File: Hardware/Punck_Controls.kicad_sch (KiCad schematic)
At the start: 38 parts, among them J1 Conn_01x12_Female, J10 Conn_01x12_Female, J11 Tempo_Out, J12 USB_B_Micro, J13 Midi_In_L, J14 Audio_Out_L, J15 Audio_Out_R, J2 Conn_01x12_Female, J3 Conn_01x12_Female, J4 Kick_In, J5 Snare_In, J6 CH_In, J7 OH_In, J8 SamplerA_In, J9 SamplerB_In

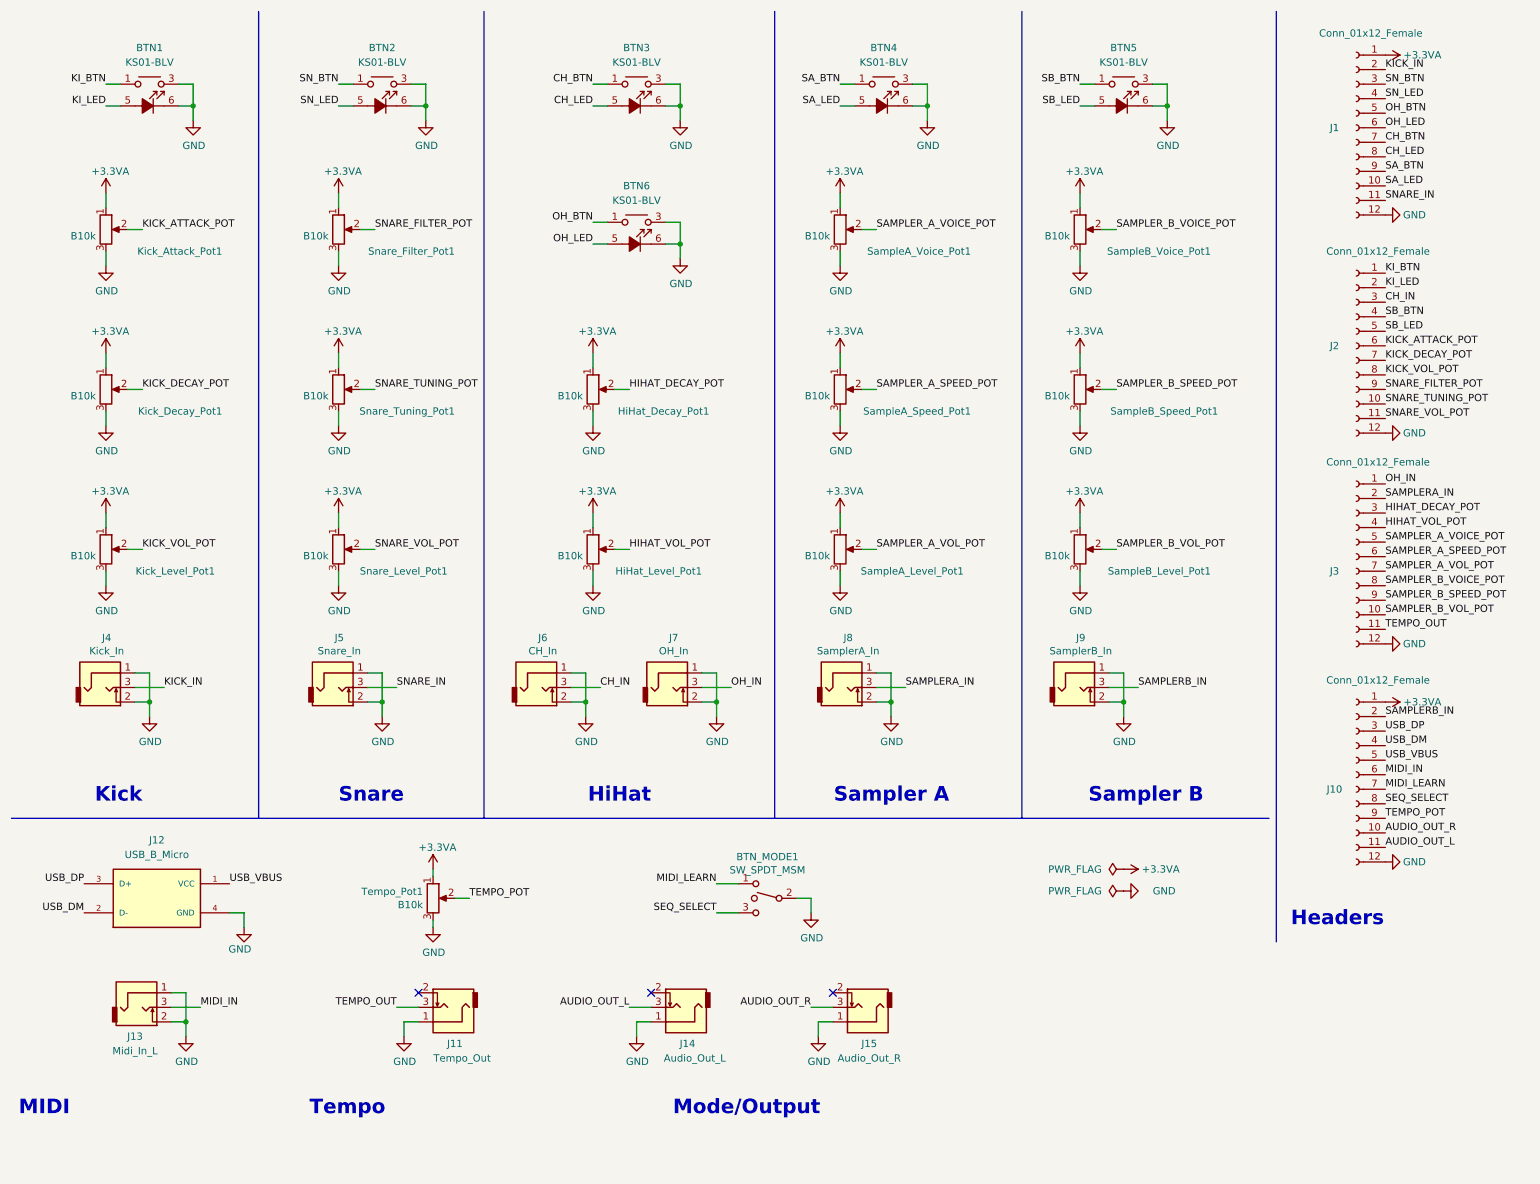
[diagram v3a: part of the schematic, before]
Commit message: Component PCB Signal routing first draft
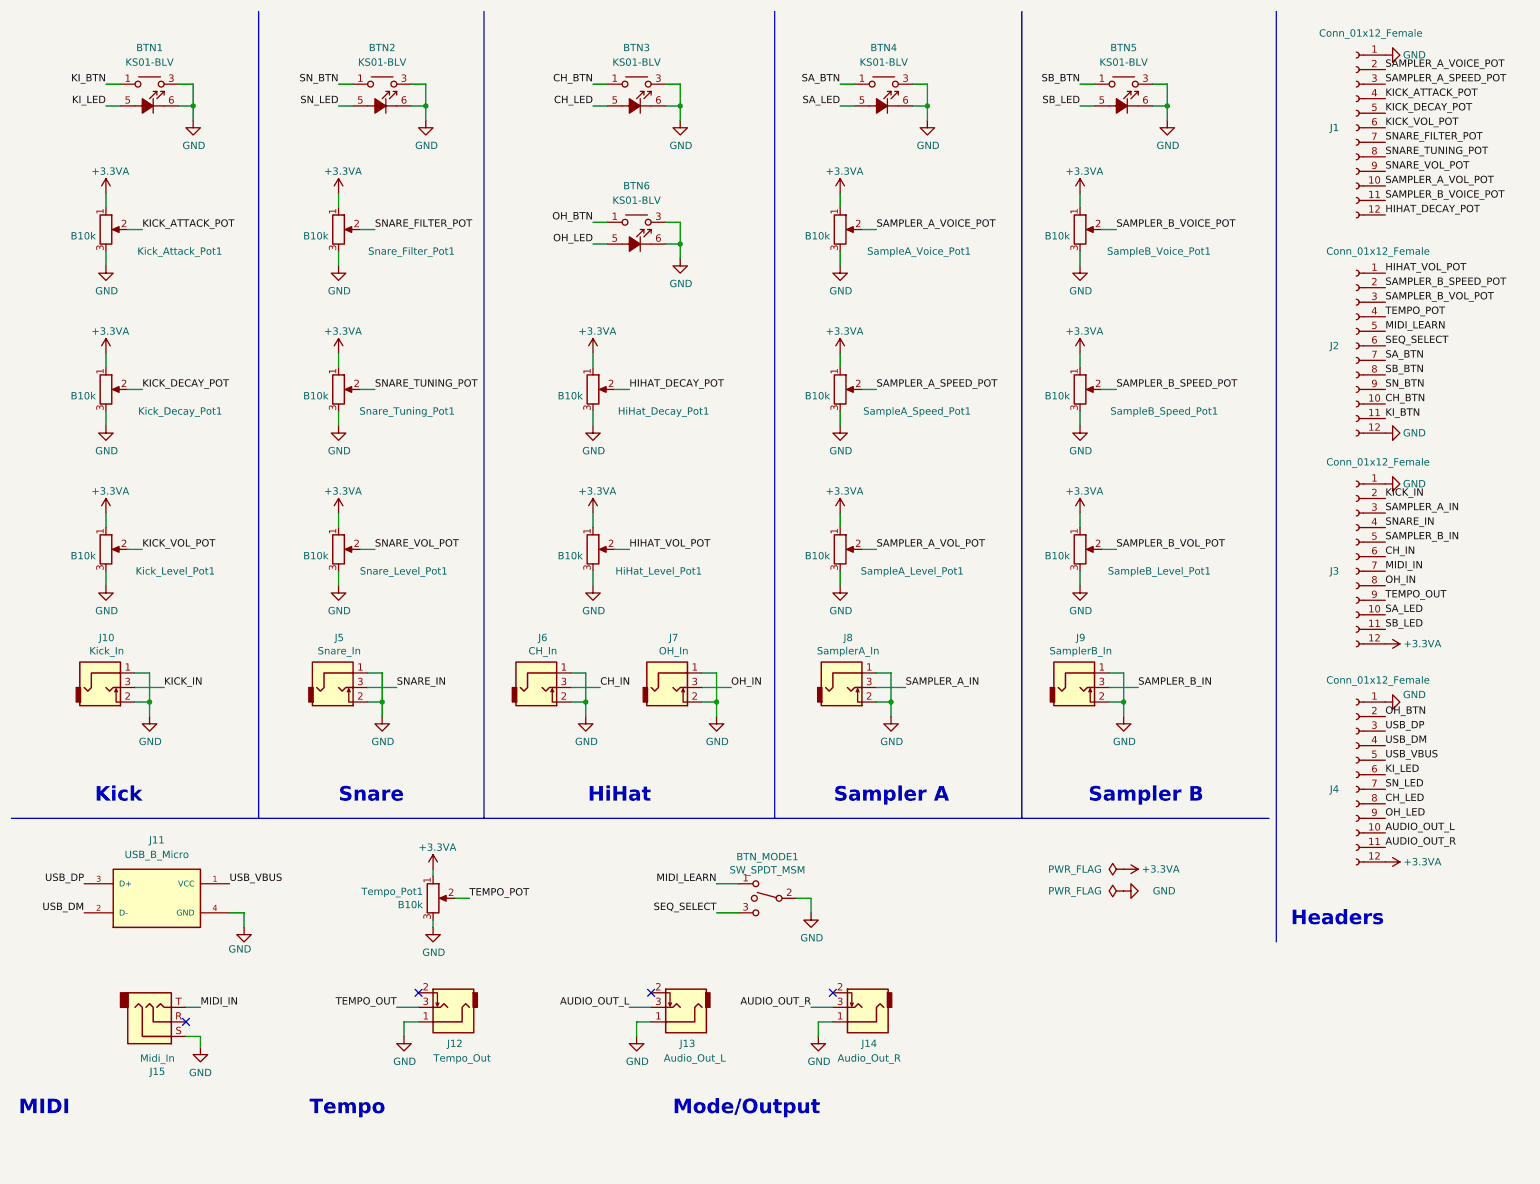
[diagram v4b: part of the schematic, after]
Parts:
- removed J13: Midi_In_L, Custom_Footprints:THONKICONN_hole, symbol thonkiconn:AudioJack2_Ground_Switch
- added J15: Midi_In, Custom_Footprints:Thonkiconn_Stereo-PJ366ST, symbol thonkiconn:AudioJack3
- renumbered J4 to J10, J12 to J11, J11 to J12, J14 to J13, J15 to J14, J10 to J4
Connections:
- net +3.3VA: now also J3.12 (Pin_12), J4.12 (Pin_12); no longer J1.1 (Pin_1), J4.1 (Pin_1)
- net AUDIO_OUT_L: now also J4.10 (Pin_10); no longer J4.11 (Pin_11)
- net AUDIO_OUT_R: now also J4.11 (Pin_11); no longer J4.10 (Pin_10)
- net CH_BTN: now also J2.10 (Pin_10); no longer J1.7 (Pin_7)
- net CH_IN: now also J3.6 (Pin_6); no longer J2.3 (Pin_3)
- net CH_LED: now also J4.8 (Pin_8); no longer J1.8 (Pin_8)
- net GND: now also J1.1 (Pin_1), J3.1 (Pin_1), J4.1 (Pin_1), J15.S; no longer J1.12 (Pin_12), J3.12 (Pin_12), J4.12 (Pin_12)
- net HIHAT_DECAY_POT: now also J1.12 (Pin_12); no longer J3.3 (Pin_3)
- net HIHAT_VOL_POT: now also J2.1 (Pin_1); no longer J3.4 (Pin_4)
- net KICK_ATTACK_POT: now also J1.4 (Pin_4); no longer J2.6 (Pin_6)
- net KICK_DECAY_POT: now also J1.5 (Pin_5); no longer J2.7 (Pin_7)
- net KICK_IN: now also J3.2 (Pin_2); no longer J1.2 (Pin_2)
- net KICK_VOL_POT: now also J1.6 (Pin_6); no longer J2.8 (Pin_8)
- net KI_BTN: now also J2.11 (Pin_11); no longer J2.1 (Pin_1)
- net KI_LED: now also J4.6 (Pin_6); no longer J2.2 (Pin_2)
- net MIDI_IN: now also J3.7 (Pin_7), J15.T; no longer J4.6 (Pin_6)
- net MIDI_LEARN: now also J2.5 (Pin_5); no longer J4.7 (Pin_7)
- net OH_BTN: now also J4.2 (Pin_2); no longer J1.5 (Pin_5)
- net OH_IN: now also J3.8 (Pin_8); no longer J3.1 (Pin_1)
- net OH_LED: now also J4.9 (Pin_9); no longer J1.6 (Pin_6)
- net SAMPLER_A_SPEED_POT: now also J1.3 (Pin_3); no longer J3.6 (Pin_6)
- net SAMPLER_A_VOICE_POT: now also J1.2 (Pin_2); no longer J3.5 (Pin_5)
- net SAMPLER_A_VOL_POT: now also J1.10 (Pin_10); no longer J3.7 (Pin_7)
- net SAMPLER_B_SPEED_POT: now also J2.2 (Pin_2); no longer J3.9 (Pin_9)
- net SAMPLER_B_VOICE_POT: now also J1.11 (Pin_11); no longer J3.8 (Pin_8)
- net SAMPLER_B_VOL_POT: now also J2.3 (Pin_3); no longer J3.10 (Pin_10)
- net SA_BTN: now also J2.7 (Pin_7); no longer J1.9 (Pin_9)
- net SA_LED: now also J3.10 (Pin_10); no longer J1.10 (Pin_10)
- net SB_BTN: now also J2.8 (Pin_8); no longer J2.4 (Pin_4)
- net SB_LED: now also J3.11 (Pin_11); no longer J2.5 (Pin_5)
- net SEQ_SELECT: now also J2.6 (Pin_6); no longer J4.8 (Pin_8)
- net SNARE_FILTER_POT: now also J1.7 (Pin_7); no longer J2.9 (Pin_9)
- net SNARE_IN: now also J3.4 (Pin_4); no longer J1.11 (Pin_11)
- net SNARE_TUNING_POT: now also J1.8 (Pin_8); no longer J2.10 (Pin_10)
- net SNARE_VOL_POT: now also J1.9 (Pin_9); no longer J2.11 (Pin_11)
- net SN_BTN: now also J2.9 (Pin_9); no longer J1.3 (Pin_3)
- net SN_LED: now also J4.7 (Pin_7); no longer J1.4 (Pin_4)
- net TEMPO_OUT: now also J3.9 (Pin_9); no longer J3.11 (Pin_11)
- net TEMPO_POT: now also J2.4 (Pin_4); no longer J4.9 (Pin_9)
- net SAMPLERA_IN renamed SAMPLER_A_IN
- net SAMPLER_A_IN: now also J3.3 (Pin_3); no longer J3.2 (Pin_2)
- net SAMPLERB_IN renamed SAMPLER_B_IN
- net SAMPLER_B_IN: now also J3.5 (Pin_5); no longer J4.2 (Pin_2)
- no-connect marks 3 -> 4

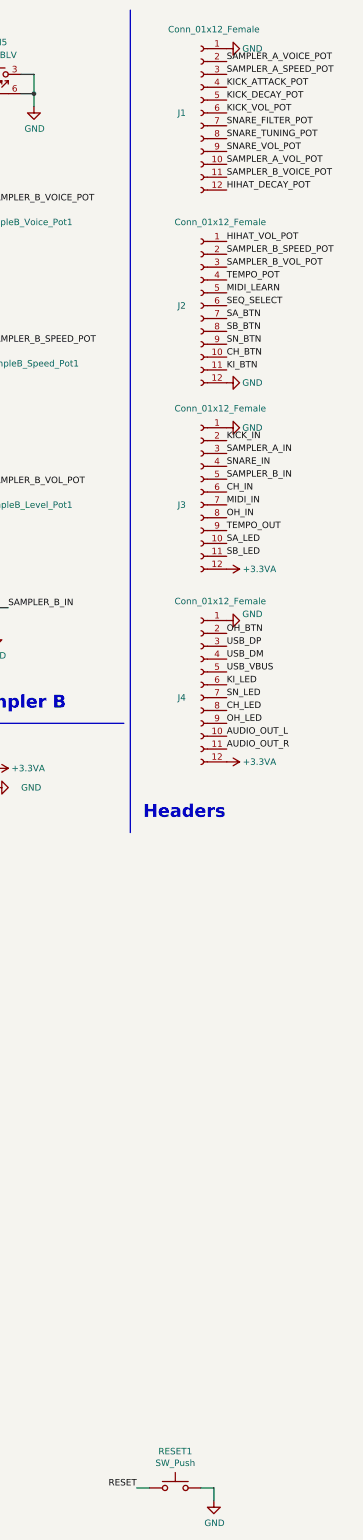
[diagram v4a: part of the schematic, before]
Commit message: Component PCB first draft
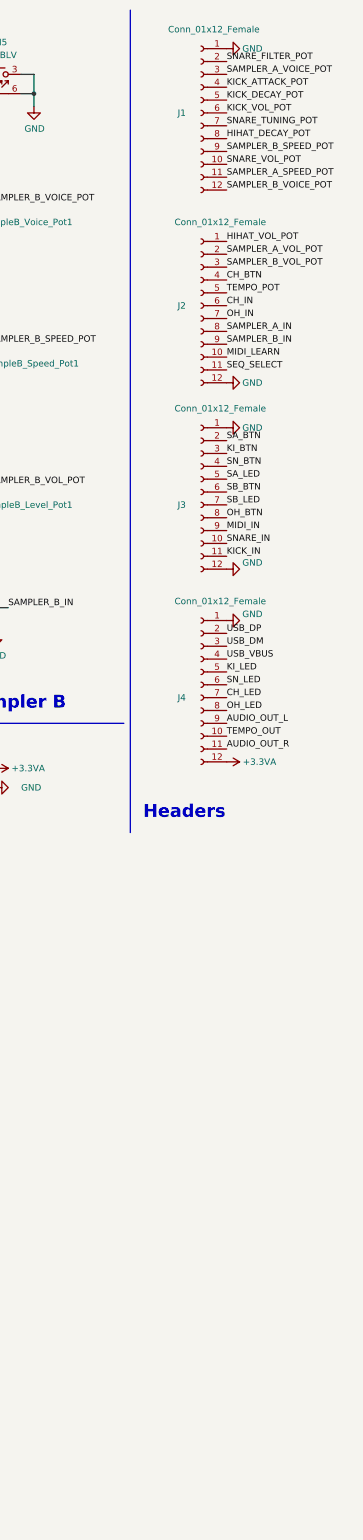
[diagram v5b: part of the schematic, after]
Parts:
- removed RESET1: SW_Push, Custom_Footprints:SW_PUSH_6mm_aligned, symbol Switch:SW_Push
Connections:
- net +3.3VA: no longer J3.12 (Pin_12)
- net AUDIO_OUT_L: now also J4.9 (Pin_9); no longer J4.10 (Pin_10)
- net CH_BTN: now also J2.4 (Pin_4); no longer J2.10 (Pin_10)
- net CH_IN: now also J2.6 (Pin_6); no longer J3.6 (Pin_6)
- net CH_LED: now also J4.7 (Pin_7); no longer J4.8 (Pin_8)
- net GND: now also J3.12 (Pin_12)
- net HIHAT_DECAY_POT: now also J1.8 (Pin_8); no longer J1.12 (Pin_12)
- net KICK_IN: now also J3.11 (Pin_11); no longer J3.2 (Pin_2)
- net KI_BTN: now also J3.3 (Pin_3); no longer J2.11 (Pin_11)
- net KI_LED: now also J4.5 (Pin_5); no longer J4.6 (Pin_6)
- net MIDI_IN: now also J3.9 (Pin_9); no longer J3.7 (Pin_7)
- net MIDI_LEARN: now also J2.10 (Pin_10); no longer J2.5 (Pin_5)
- net OH_BTN: now also J3.8 (Pin_8); no longer J4.2 (Pin_2)
- net OH_IN: now also J2.7 (Pin_7); no longer J3.8 (Pin_8)
- net OH_LED: now also J4.8 (Pin_8); no longer J4.9 (Pin_9)
- net SAMPLER_A_IN: now also J2.8 (Pin_8); no longer J3.3 (Pin_3)
- net SAMPLER_A_SPEED_POT: now also J1.11 (Pin_11); no longer J1.3 (Pin_3)
- net SAMPLER_A_VOICE_POT: now also J1.3 (Pin_3); no longer J1.2 (Pin_2)
- net SAMPLER_A_VOL_POT: now also J2.2 (Pin_2); no longer J1.10 (Pin_10)
- net SAMPLER_B_IN: now also J2.9 (Pin_9); no longer J3.5 (Pin_5)
- net SAMPLER_B_SPEED_POT: now also J1.9 (Pin_9); no longer J2.2 (Pin_2)
- net SAMPLER_B_VOICE_POT: now also J1.12 (Pin_12); no longer J1.11 (Pin_11)
- net SA_BTN: now also J3.2 (Pin_2); no longer J2.7 (Pin_7)
- net SA_LED: now also J3.5 (Pin_5); no longer J3.10 (Pin_10)
- net SB_BTN: now also J3.6 (Pin_6); no longer J2.8 (Pin_8)
- net SB_LED: now also J3.7 (Pin_7); no longer J3.11 (Pin_11)
- net SEQ_SELECT: now also J2.11 (Pin_11); no longer J2.6 (Pin_6)
- net SNARE_FILTER_POT: now also J1.2 (Pin_2); no longer J1.7 (Pin_7)
- net SNARE_IN: now also J3.10 (Pin_10); no longer J3.4 (Pin_4)
- net SNARE_TUNING_POT: now also J1.7 (Pin_7); no longer J1.8 (Pin_8)
- net SNARE_VOL_POT: now also J1.10 (Pin_10); no longer J1.9 (Pin_9)
- net SN_BTN: now also J3.4 (Pin_4); no longer J2.9 (Pin_9)
- net SN_LED: now also J4.6 (Pin_6); no longer J4.7 (Pin_7)
- net TEMPO_OUT: now also J4.10 (Pin_10); no longer J3.9 (Pin_9)
- net TEMPO_POT: now also J2.5 (Pin_5); no longer J2.4 (Pin_4)
- net USB_DM: now also J4.3 (Pin_3); no longer J4.4 (Pin_4)
- net USB_DP: now also J4.2 (Pin_2); no longer J4.3 (Pin_3)
- net USB_VBUS: now also J4.4 (Pin_4); no longer J4.5 (Pin_5)

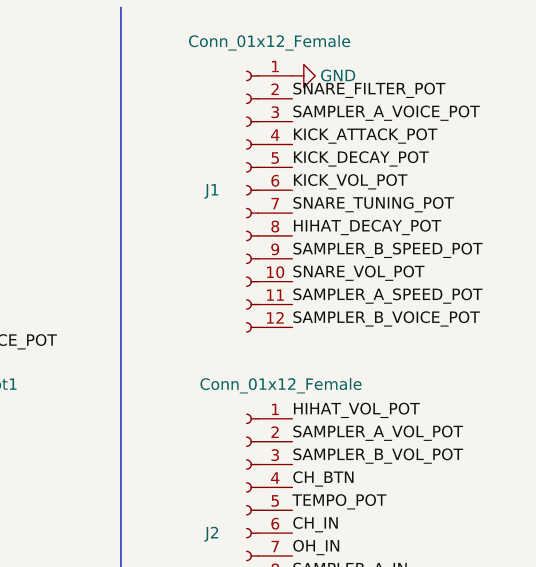
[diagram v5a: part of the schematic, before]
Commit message: Updated components on panel board
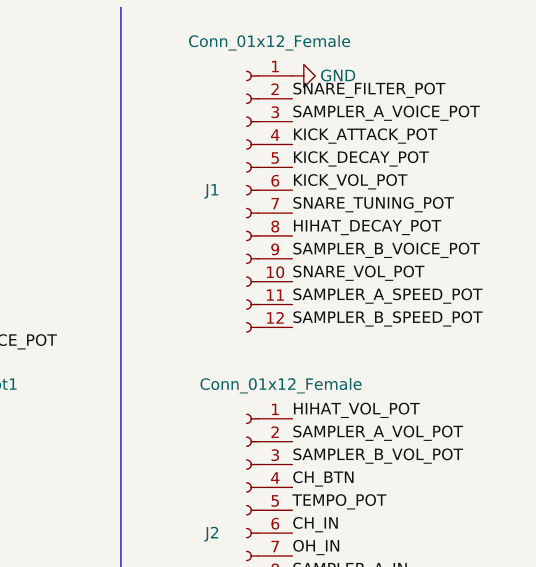
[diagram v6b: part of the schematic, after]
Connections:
- net SAMPLER_B_SPEED_POT: now also J1.12 (Pin_12); no longer J1.9 (Pin_9)
- net SAMPLER_B_VOICE_POT: now also J1.9 (Pin_9); no longer J1.12 (Pin_12)
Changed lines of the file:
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@@
     (effects (font (size 1.27 1.27)) (justify left bottom))
   )
-  (label "SAMPLER_B_SPEED_POT" (at 252.73 40.64 0)
+  (label "SAMPLER_B_SPEED_POT" (at 252.73 48.26 0)
     (effects (font (size 1.27 1.27)) (justify left bottom))
   )
@@
     (effects (font (size 1.27 1.27)) (justify left bottom))
   )
-  (label "SAMPLER_B_VOICE_POT" (at 252.73 48.26 0)
+  (label "SAMPLER_B_VOICE_POT" (at 252.73 40.64 0)
     (effects (font (size 1.27 1.27)) (justify left bottom))
   )
